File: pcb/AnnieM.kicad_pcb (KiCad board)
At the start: 2 copper layers, 28 parts, among them J1 NRG200P, J2 NRG400, J3 SOLAR, J4 ARDUCAM, U1 BME688, U2 ICARUS_IOT_BOARD_TH, U3 LM393

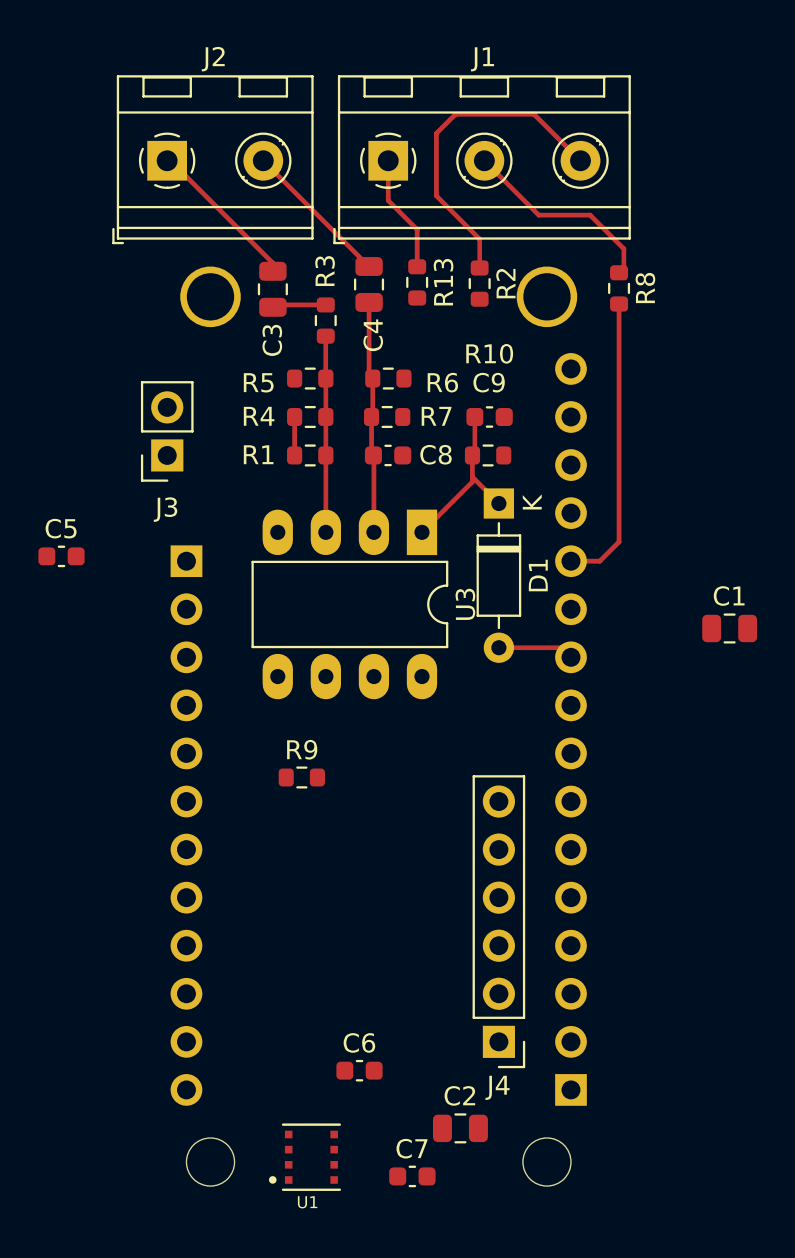
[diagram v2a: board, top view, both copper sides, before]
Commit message: relayout, new temp and camera connection
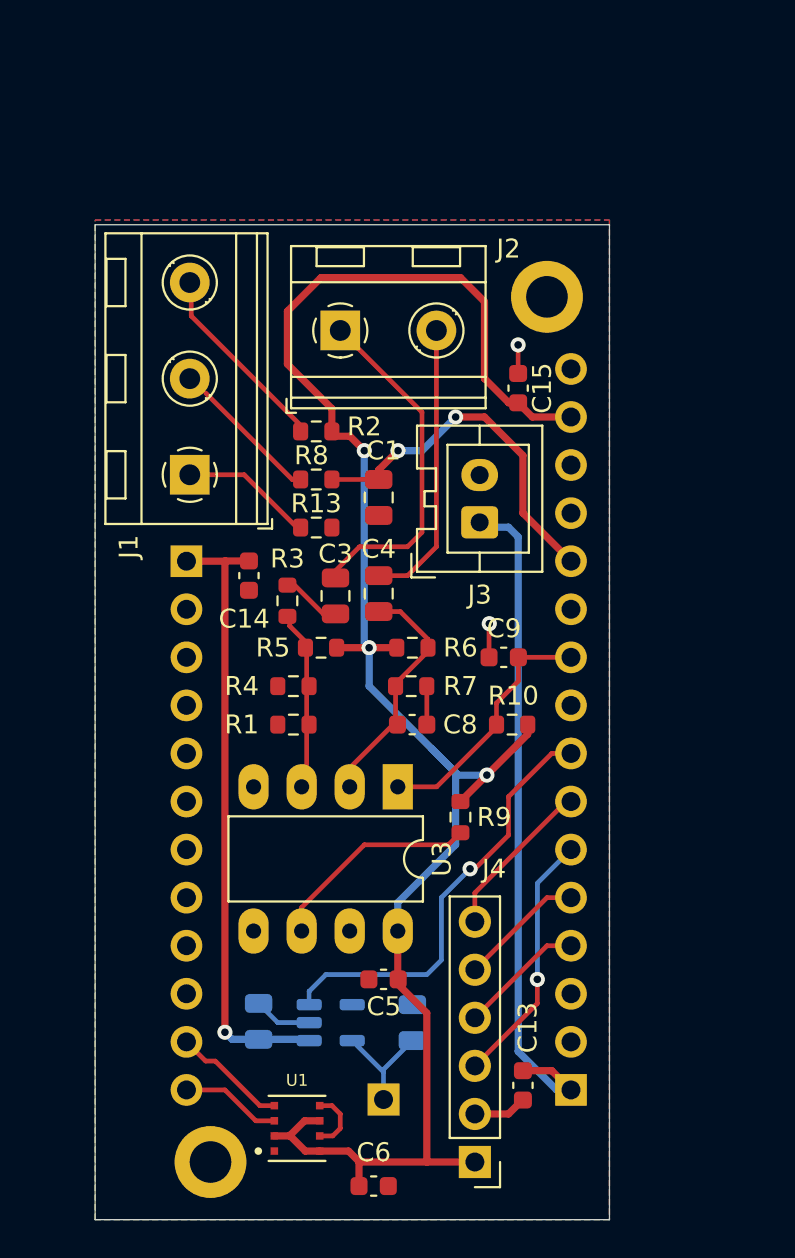
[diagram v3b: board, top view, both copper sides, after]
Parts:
- removed C2: 10uf, Capacitor_SMD:C_0805_2012Metric
- removed C7: 0.1uf, Capacitor_SMD:C_0603_1608Metric
- removed D1: 1N914, Diode_THT:D_DO-35_SOD27_P7.62mm_Horizontal
- added C10: 1uf, Capacitor_SMD:C_0805_2012Metric, B.Cu at (178.1, 99.2)
- added C11: 10uf, Capacitor_SMD:C_0805_2012Metric, B.Cu at (186.2, 99.3)
- added C13: 0.1uf, Capacitor_SMD:C_0603_1608Metric, F.Cu at (192.0, 102.6)
- added C14: 0.1uf, Capacitor_SMD:C_0603_1608Metric, F.Cu at (177.5, 75.7)
- added C15: 0.1uf, Capacitor_SMD:C_0603_1608Metric, F.Cu at (191.8, 65.8)
- added H1: , MountingHole:MountingHole_2.2mm_M2_DIN965_Pad, F.Cu at (193.3, 61.0)
- added H2: , MountingHole:MountingHole_2.2mm_M2_DIN965_Pad, F.Cu at (175.5, 106.7)
- added J5: Ext_3.3V, Connector_PinSocket_2.54mm:PinSocket_1x01_P2.54mm_Vertical, B.Cu at (184.7, 103.4)
- added U4: RT9080-33GJ5, Package_TO_SOT_SMD:TSOT-23-5, B.Cu at (181.9, 99.3)
- J3: footprint Connector_PinSocket_2.54mm:PinSocket_1x02_P2.54mm_Vertical -> Connector_JST:JST_XA_B02B-XASK-1_1x02_P2.50mm_Vertical
- U1: value BME688 -> BME688az
- U2: value ICARUS_IOT_BOARD_TH -> ICARUS_IOT_BOARD_THaz; footprint ICARUS_IOT_BOARD_TH:MODULE_ICARUS_IOT_BOARD_TH -> ICARUS_IOT_BOARD_TH:MODULE_ICARUS_IOT_BOARD_THaz
- moved C5 28.1 mm to (184.7, 97.0), turned to 180 degrees
- moved C1 19.8 mm to (184.4, 71.6), turned to 90 degrees
- moved J1 19.6 mm to (174.4, 70.4), turned to 90 degrees
- moved R8 18.9 mm to (181.1, 70.6), turned to 0 degrees
- moved J3 16.9 mm to (189.7, 72.9), turned to 90 degrees
- moved C3 16.5 mm to (182.1, 76.8)
- moved C4 16.3 mm to (184.4, 76.6)
- moved R3 14.9 mm to (179.6, 77.0)
- moved C8 14.3 mm to (186.2, 83.6)
- moved R10 14.3 mm to (191.5, 83.6)
- moved R7 14.3 mm to (186.1, 81.5)
- moved R6 14.3 mm to (186.2, 79.5), turned to 0 degrees
- moved R1 14.3 mm to (179.9, 83.6)
- moved R4 14.3 mm to (179.9, 81.5)
- moved R5 14.2 mm to (181.4, 79.5), turned to 0 degrees
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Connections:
- C9 pad 2: Net-(C9-Pad2) -> SPEED
- R10 pad 1: Net-(C9-Pad2) -> SPEED
- U2 pad JP1_8: unconnected-(U2-PadJP1_8) -> EXT_3V_EN
- U3 pad 1: Net-(C9-Pad2) -> SPEED
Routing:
- net VCC: track 0.00 -> 98.8 mm, vias 0 -> 3
- net +10V: track 0.00 -> 35.8 mm
- net +BATT: track 0.00 -> 32.7 mm, vias 0 -> 1
- net EXT_3V_EN: track 0.00 -> 22.9 mm, vias 0 -> 1
- net SCK: track 0.00 -> 13.5 mm, vias 0 -> 1
- net GND: track 2.03 -> 14.5 mm, vias 0 -> 2
- net Net-(R9-Pad1): track 0.00 -> 11.3 mm
- net Net-(C3-Pad2): track 8.26 -> 17.9 mm
- net SPEED: track 4.02 -> 13.3 mm
- net Net-(C9-Pad2): track 9.23 -> 0.00 mm
- net CAMERA_CS: track 0.00 -> 8.35 mm
- net Net-(J1-Pad3): track 17.1 -> 9.08 mm
- net Net-(C4-Pad2): track 7.90 -> 15.1 mm
- net MOSI: track 0.00 -> 6.66 mm
- net MISO: track 0.00 -> 6.66 mm
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- added copper zone on B.Cu, net GND
- added copper zone on F.Cu, net GND
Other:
- board outline added: 27.2 x 52.6 mm

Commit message: Reordered annotations graphically
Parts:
- renumbered C15 to C1, C6 to C10, C10 to C12, C1 to C2, C14 to C3, C3 to C4, C4 to C5, C9 to C6, C8 to C7, C5 to C8, C13 to C9, J2 to J1, J1 to J2, R2 to R1, R9 to R11, R8 to R2, R13 to R3, R3 to R4, R4 to R7, R7 to R8, R1 to R9, U3 to U1, U1 to U2, U2 to U3
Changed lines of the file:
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@@
     (property "Sheetname" "")
     (attr smd)
-    (fp_text reference "R9" (at 0 1.778 180) (layer "F.SilkS")
+    (fp_text reference "R11" (at 0 1.778 180) (layer "F.SilkS")
       (effects (font (size 1 1) (thickness 0.15)))
     )
@@
     (property "Sheetname" "")
     (attr smd)
-    (fp_text reference "R8" (at -0.254 -1.27) (layer "F.SilkS")
+    (fp_text reference "R2" (at -0.254 -1.27) (layer "F.SilkS")
       (effects (font (size 1 1) (thickness 0.15)))
     )
@@
     (property "Sheetname" "")
     (attr smd)
-    (fp_text reference "C14" (at 2.286 0.254 180) (layer "F.SilkS")
+    (fp_text reference "C3" (at 2.286 0.254 180) (layer "F.SilkS")
       (effects (font (size 1 1) (thickness 0.15)))
     )
@@
     (property "Sheetname" "")
     (attr smd)
-    (fp_text reference "R13" (at 0 -1.27) (layer "F.SilkS")
+    (fp_text reference "R3" (at 0 -1.27) (layer "F.SilkS")
       (effects (font (size 1 1) (thickness 0.15)))
     )
@@
     (property "Sheetname" "")
     (attr smd)
-    (fp_text reference "C6" (at 0 1.778) (layer "F.SilkS")
+    (fp_text reference "C10" (at 0 1.778) (layer "F.SilkS")
       (effects (font (size 1 1) (thickness 0.15)))
     )
@@
     (property "Sheetname" "")
     (attr through_hole)
-    (fp_text reference "J2" (at 8.89 -4.318) (layer "F.SilkS")
+    (fp_text reference "J1" (at 8.89 -4.318) (layer "F.SilkS")
       (effects (font (size 1 1) (thickness 0.15)))
     )
@@
     (fp_line (start -1.25 -4.4) (end 1.25 -4.4) (layer "F.SilkS") (width 0.12))
     (fp_line (start 3.83 -4.4) (end 3.83 -3.4) (layer "F.SilkS") (width 0.12))
-    (fp_arc (start -0.627362 -1.285823) (mid -0.000201 -1.430702) (end 0.627 -1.286) (layer "F.SilkS") (width 0.12))
+    (fp_arc (start -0.627362 -1.285823) (mid -0.000201 -1.430701) (end 0.627 -1.286) (layer "F.SilkS") (width 0.12))
     (fp_arc (start 0.02428 1.43094) (mid -0.310437 1.397071) (end -0.628 1.286) (layer "F.SilkS") (width 0.12))
     (fp_arc (start 0.626871 1.285275) (mid 0.32168 1.393349) (end 0 1.43) (layer "F.SilkS") (width 0.12))
@@
     (property "Sheetname" "")
     (attr smd)
-    (fp_text reference "C1" (at 2.474 0.254 180) (layer "F.SilkS")
+    (fp_text reference "C2" (at 2.474 0.254 180) (layer "F.SilkS")
       (effects (font (size 1 1) (thickness 0.15)))
     )
@@
     (property "Sheetname" "")
     (attr through_hole)
-    (fp_text reference "J1" (at -3.805 -3.223 90) (layer "F.SilkS")
+    (fp_text reference "J2" (at -3.805 -3.223 90) (layer "F.SilkS")
       (effects (font (size 1 1) (thickness 0.15)))
     )
@@
     (fp_arc (start 0.626871 1.285275) (mid 0.32168 1.393349) (end 0 1.43) (layer "F.SilkS") (width 0.12))
     (fp_arc (start -1.286611 0.626746) (mid -1.431146 -0.000698) (end -1.286 -0.628) (layer "F.SilkS") (width 0.12))
-    (fp_arc (start -0.627362 -1.285823) (mid -0.000201 -1.430702) (end 0.627 -1.286) (layer "F.SilkS") (width 0.12))
+    (fp_arc (start -0.627362 -1.285823) (mid -0.000201 -1.430701) (end 0.627 -1.286) (layer "F.SilkS") (width 0.12))
     (fp_arc (start 0.02428 1.43094) (mid -0.310437 1.397071) (end -0.628 1.286) (layer "F.SilkS") (width 0.12))
     (fp_arc (start 1.285823 -0.627362) (mid 1.430707 -0.000201) (end 1.286 0.627) (layer "F.SilkS") (width 0.12))
@@
     (property "Sheetname" "")
     (attr smd)
-    (fp_text reference "C13" (at -3.048 -0.254 -90) (layer "F.SilkS")
+    (fp_text reference "C9" (at -3.048 -0.254 -90) (layer "F.SilkS")
       (effects (font (size 1 1) (thickness 0.15)))
     )
@@
     (property "Sheetname" "")
     (attr smd)
-    (fp_text reference "R3" (at 2.223 0 180) (layer "F.SilkS")
+    (fp_text reference "R4" (at 2.223 0 180) (layer "F.SilkS")
       (effects (font (size 1 1) (thickness 0.15)))
     )
@@
     (property "Sheetname" "")
     (attr smd)
-    (fp_text reference "R1" (at -2.731 0) (layer "F.SilkS")
+    (fp_text reference "R9" (at -2.731 0) (layer "F.SilkS")
       (effects (font (size 1 1) (thickness 0.15)))
     )
@@
     (property "Sheetname" "")
     (attr smd)
-    (fp_text reference "C5" (at -0.013 -1.43) (layer "F.SilkS")
+    (fp_text reference "C8" (at -0.013 -1.43) (layer "F.SilkS")
       (effects (font (size 1 1) (thickness 0.15)))
     )
@@
     (property "Sheetname" "")
     (attr smd)
-    (fp_text reference "C9" (at 0.013 -1.524) (layer "F.SilkS")
+    (fp_text reference "C6" (at 0.013 -1.524) (layer "F.SilkS")
       (effects (font (size 1 1) (thickness 0.15)))
     )
@@
     (property "Sheetname" "")
     (attr smd)
-    (fp_text reference "C8" (at -2.54 0) (layer "F.SilkS")
+    (fp_text reference "C7" (at -2.54 0) (layer "F.SilkS")
       (effects (font (size 1 1) (thickness 0.15)))
     )
@@
     (property "Sheetname" "")
     (attr smd)
-    (fp_text reference "C15" (at 0 -1.27 90) (layer "F.SilkS")
+    (fp_text reference "C1" (at 0 -1.27 90) (layer "F.SilkS")
       (effects (font (size 1 1) (thickness 0.15)))
     )
@@
     (property "Sheetname" "")
     (attr smd)
-    (fp_text reference "R4" (at -2.731 0) (layer "F.SilkS")
+    (fp_text reference "R7" (at -2.731 0) (layer "F.SilkS")
       (effects (font (size 1 1) (thickness 0.15)))
     )
@@
     (property "Sheetname" "")
     (attr smd)
-    (fp_text reference "C4" (at 2.352 0 180) (layer "F.SilkS")
+    (fp_text reference "C5" (at 2.352 0 180) (layer "F.SilkS")
       (effects (font (size 1 1) (thickness 0.15)))
     )
@@
     (property "Sheetname" "")
     (attr through_hole)
-    (fp_text reference "U3" (at 3.81 -2.33 90) (layer "F.SilkS")
+    (fp_text reference "U1" (at 3.81 -2.33 90) (layer "F.SilkS")
       (effects (font (size 1 1) (thickness 0.15)))
     )
@@
     (property "Sheetname" "")
     (attr smd)
-    (fp_text reference "C3" (at 2.22 0 180) (layer "F.SilkS")
+    (fp_text reference "C4" (at 2.22 0 180) (layer "F.SilkS")
       (effects (font (size 1 1) (thickness 0.15)))
     )
@@
     (property "SnapEDA_Link" "https://www.snapeda.com/parts/BME688/Bosch+Sensortec/view-part/?ref=snap")
     (attr smd)
-    (fp_text reference "U1" (at 0 2.54) (layer "F.SilkS")
+    (fp_text reference "U2" (at 0 2.54) (layer "F.SilkS")
       (effects (font (size 0.629921 0.629921) (thickness 0.15)))
     )
@@
     (property "Sheetname" "")
     (attr smd)
-    (fp_text reference "R7" (at 2.603 0) (layer "F.SilkS")
+    (fp_text reference "R8" (at 2.603 0) (layer "F.SilkS")
       (effects (font (size 1 1) (thickness 0.15)))
     )
@@
     (property "Sheetname" "")
     (attr smd)
-    (fp_text reference "R2" (at 2.54 -0.254) (layer "F.SilkS")
+    (fp_text reference "R1" (at 2.54 -0.254) (layer "F.SilkS")
       (effects (font (size 1 1) (thickness 0.15)))
     )
@@
     (property "SnapEDA_Link" "https://www.snapeda.com/parts/Icarus%20IoT%20Board/Actinius/view-part/?ref=snap")
     (attr through_hole)
-    (fp_text reference "U2" (at -20.955 13.335 90) (layer "B.SilkS")
+    (fp_text reference "U3" (at -20.955 13.335 90) (layer "B.SilkS")
       (effects (font (size 1 1) (thickness 0.15)) (justify mirror))
     )
@@
     (property "Sheetname" "")
     (attr smd)
-    (fp_text reference "C10" (at 2.22 0) (layer "B.SilkS")
+    (fp_text reference "C12" (at 2.22 0) (layer "B.SilkS")
       (effects (font (size 1 1) (thickness 0.15)) (justify mirror))
     )

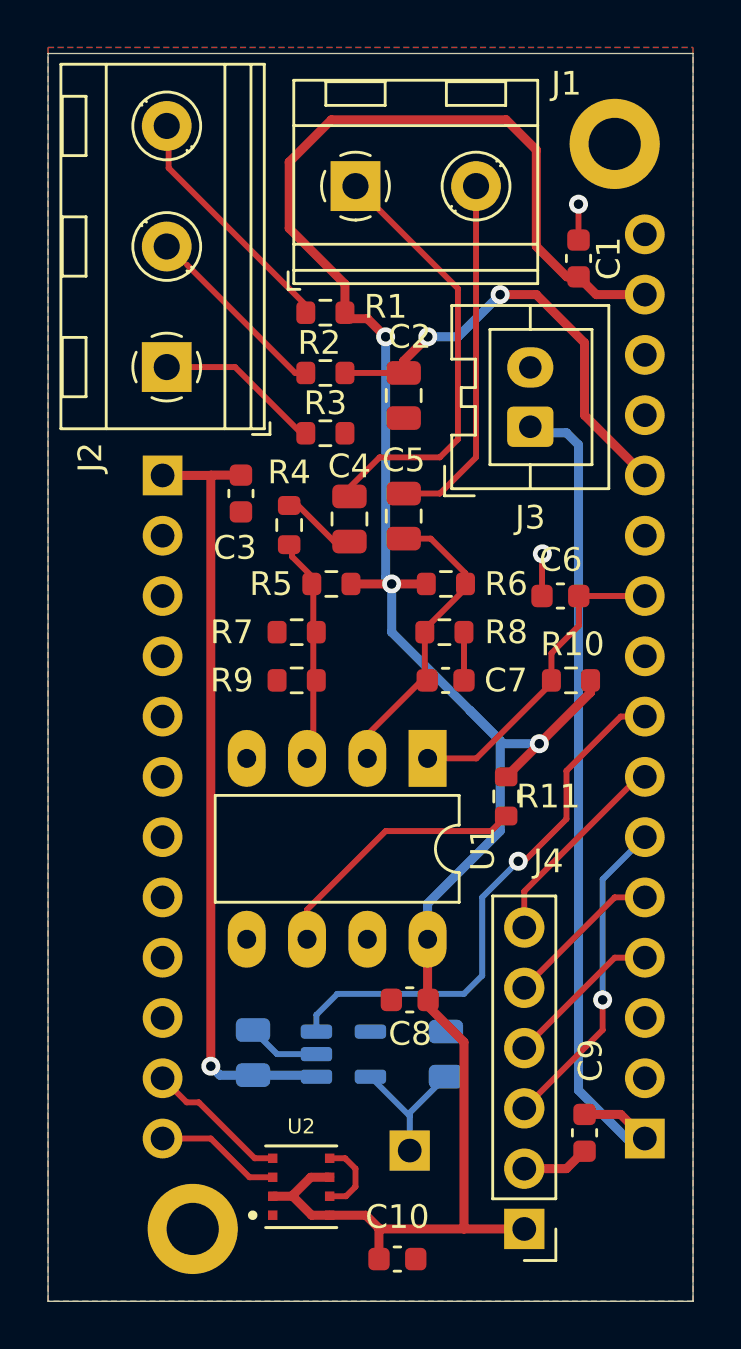
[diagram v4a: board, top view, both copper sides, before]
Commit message: changed board area to be 2"
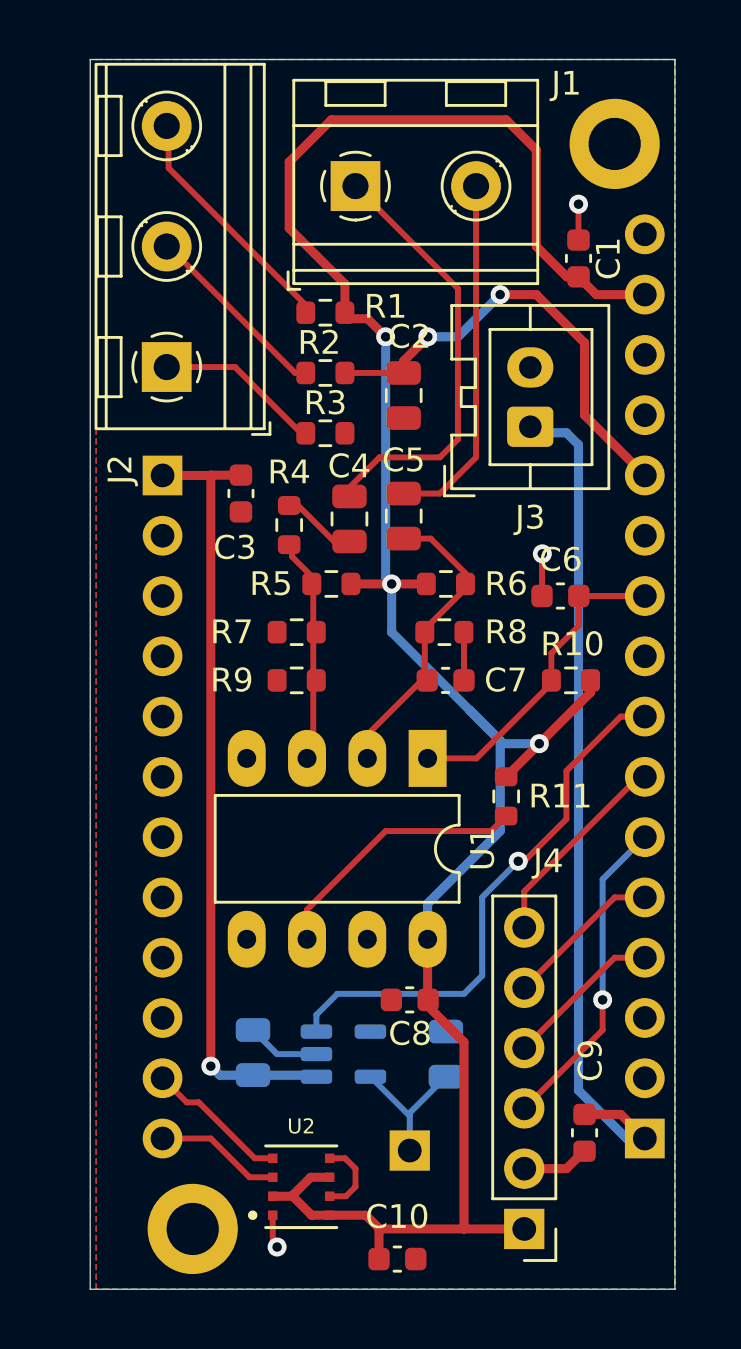
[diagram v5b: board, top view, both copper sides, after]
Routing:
- net GND: track 14.5 -> 15.9 mm, vias 2 -> 3
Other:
- board size 27.2 x 52.6 mm -> 24.6 x 51.8 mm

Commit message: Minor changes, Sent off to OSHPark
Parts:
- added J6: EXT_BME280, Connector_PinSocket_2.54mm:PinSocket_1x04_P2.54mm_Vertical, F.Cu at (171.2, 77.4)
- moved C5 2.13 mm to (186.5, 77.2), turned to 180 degrees
- moved R9 1.58 mm to (181.5, 83.4)
- moved R7 1.56 mm to (181.5, 81.5)
- moved R4 1.13 mm to (180.6, 76.7)
- moved C4 0.57 mm to (182.7, 76.6)
- moved C3 0.45 mm to (178.0, 75.5)
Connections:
- U3 pad JP3_4: unconnected-(U3-PadJP3_4) -> SDA_EX
- U3 pad JP3_5: unconnected-(U3-PadJP3_5) -> SCL_EX
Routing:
- net VCC: track 98.8 -> 112.3 mm
- net SDA_EX: track 0.00 -> 2.97 mm
- net SCL_EX: track 0.00 -> 2.97 mm
- net +BATT: track 32.7 -> 34.8 mm
- net Net-(R4-Pad1): track 8.14 -> 9.69 mm
- net GND: track 15.9 -> 17.4 mm, vias 3 -> 4
- net Net-(C5-Pad1): track 11.1 -> 9.85 mm
- net Net-(J2-Pad3): track 9.08 -> 10.3 mm
- net Net-(C4-Pad2): track 17.9 -> 16.7 mm
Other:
- board size 24.6 x 51.8 mm -> 26 x 51.8 mm
- board text added: "AnnieM V1.0"
